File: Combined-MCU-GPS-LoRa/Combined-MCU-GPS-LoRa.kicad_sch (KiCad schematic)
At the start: 0 parts

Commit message: Added Readme
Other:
- added sheet power (power.kicad_sch)
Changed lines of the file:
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@@
     )
   )
-  (sheet (at 114.3 74.93) (size 49.53 36.83) (fields_autoplaced)
+  (sheet (at 133.35 106.68) (size 49.53 36.83) (fields_autoplaced)
     (stroke (width 0.1524) (type solid))
     (fill (color 0 0 0 0.0000))
-    (property "Sheetname" "gps" (at 114.3 74.2184 0)
+    (property "Sheetname" "gps" (at 133.35 105.9684 0)
       (effects (font (size 1.27 1.27)) (justify left bottom))
     )
-    (property "Sheetfile" "gps.kicad_sch" (at 114.3 112.3446 0)
+    (property "Sheetfile" "gps.kicad_sch" (at 133.35 144.0946 0)
       (effects (font (size 1.27 1.27)) (justify left top))
     )
@@
       )
     )
+  )
+  (sheet (at 68.58 114.3) (size 36.83 33.02) (fields_autoplaced)
+    (stroke (width 0.1524) (type solid))
+    (fill (color 0 0 0 0.0000))
+    (property "Sheetname" "power" (at 68.58 113.5884 0)
+      (effects (font (size 1.27 1.27)) (justify left bottom))
+    )
+    (property "Sheetfile" "power.kicad_sch" (at 68.58 147.9046 0)
+      (effects (font (size 1.27 1.27)) (justify left top))
+    )
+    (instances
+      (project "Combined-MCU-GPS-LoRa"
+        (path "/a0175fec-7c81-4d4b-9fe1-21009e5acfd6" (page "6"))
+      )
+    )

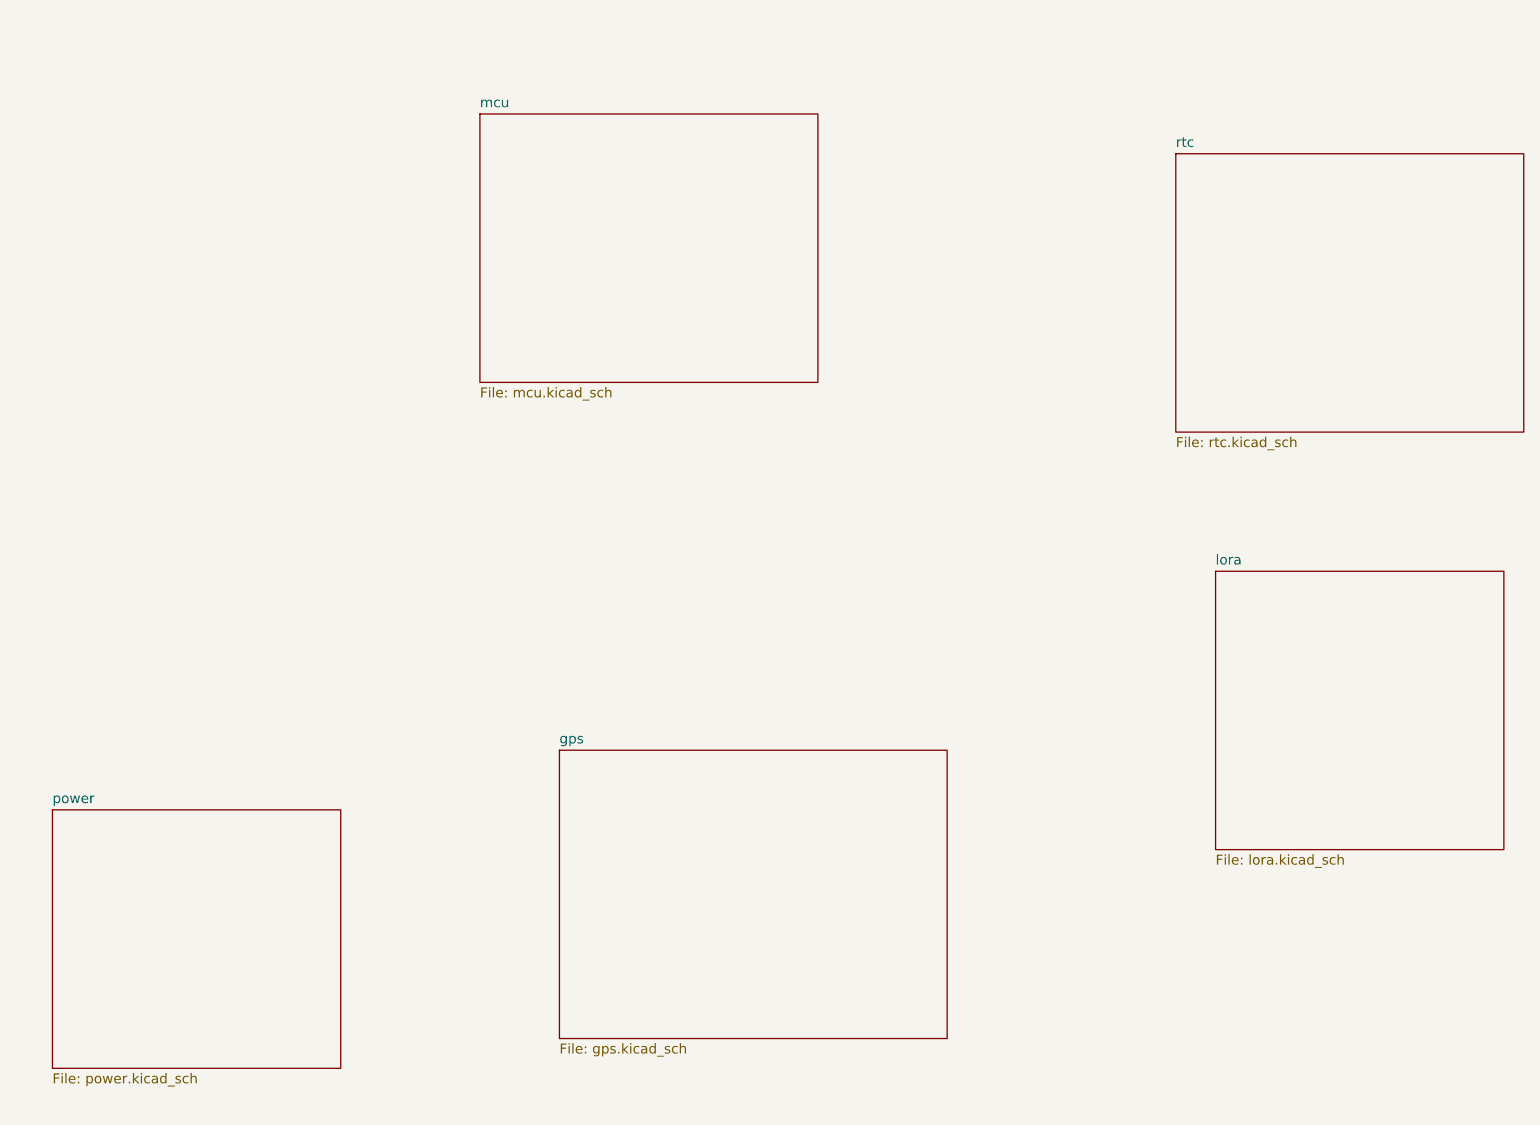
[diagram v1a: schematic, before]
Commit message: I think I have the schematic done.
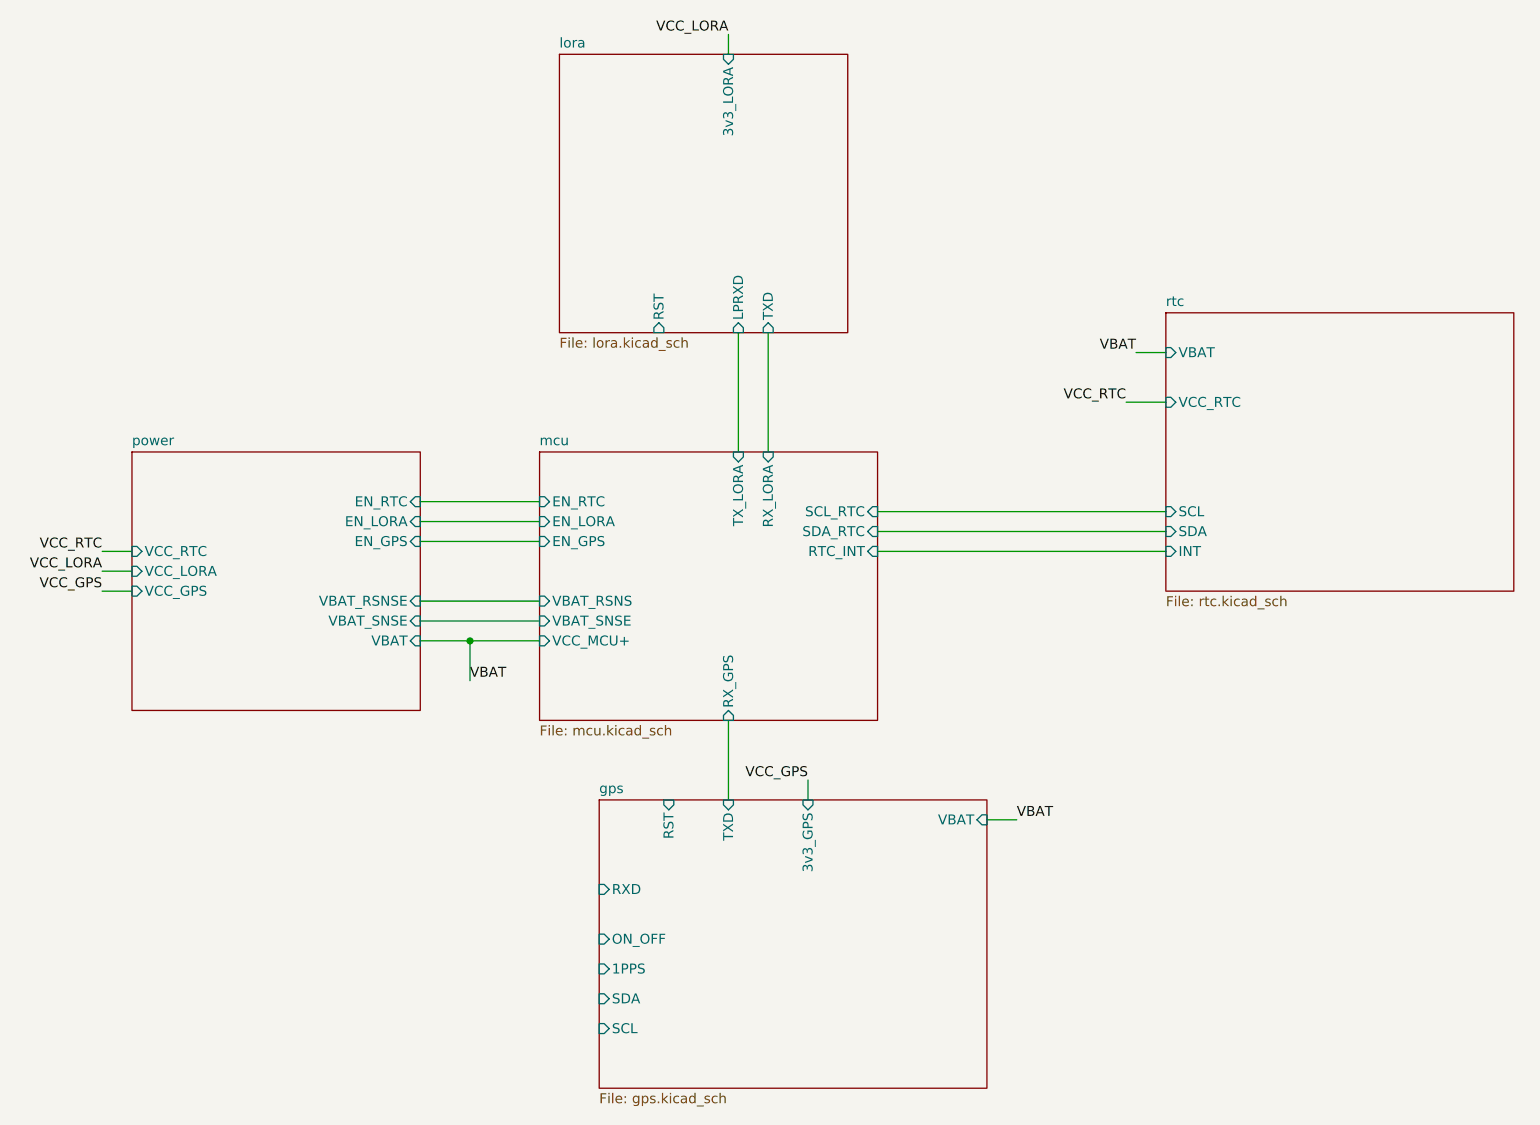
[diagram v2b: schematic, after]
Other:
- sheet gps ports: added 1PPS, 3v3_GPS, ON_OFF, RST, RXD, SCL, SDA, TXD, VBAT; removed none
- sheet lora ports: added 3v3_LORA, LPRXD, RST, TXD; removed none
- sheet mcu ports: added EN_GPS, EN_LORA, EN_RTC, RTC_INT, RX_GPS, RX_LORA, SCL_RTC, SDA_RTC, TX_LORA, VBAT_RSNS, VBAT_SNSE, VCC_MCU+; removed none
- sheet power ports: added EN_GPS, EN_LORA, EN_RTC, VBAT, VBAT_RSNSE, VBAT_SNSE, VCC_GPS, VCC_LORA, VCC_RTC; removed none
- sheet rtc ports: added INT, SCL, SDA, VBAT, VCC_RTC; removed none
